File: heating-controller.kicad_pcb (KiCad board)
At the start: 2 copper layers, 0 parts

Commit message: Place and autoroute the board; add the reproducible routing pipeline
Board 150 x 95 mm, 2-layer, routed with Freerouting 2.5 from a placed
layout: DRC 0 violations / 0 unconnected, schematic parity clean, ERC clean.

- Isolation band, antenna keep-out, relay/opto slots, 6.4 mm mains-to-SELV
  custom DRC (heating-controller.kicad_dru) and MAINS / MAINS_SENSE / Power
  net classes in the project file.
- Fixed wiring laid before routing: L/N buses, relay COM/NO links,
  DEMAND_RET return, USB-C D+/D- bridges and VBUS escape, 31 GND stitching
  vias so the bottom pour stays in one piece.
- J115/J116 moved in from the board edge so every courtyard is inside the
  outline (JLC assembly margin).
- tools/route/: prep -> Freerouting -> SES import + pours -> DRC + gap fix,
  reproducible in ~2 min; outputs land in fab/route/ (ignored).
- Schematic: pin-type fixes in the project library, ESP32 thermal pads
  numbered; docs/design.md layout section rewritten to match the board.

Co-Authored-By: Claude Fable 5.1 <noreply@anthropic.com>
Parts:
- added C1: 1nF, Capacitor_SMD:C_0603_1608Metric, F.Cu at (32.5, 80.0)
- added C10: 100nF, Capacitor_SMD:C_0603_1608Metric, F.Cu at (132.5, 83.0)
- added C101: 1uF, Capacitor_SMD:C_0603_1608Metric, F.Cu at (97.0, 64.0)
- added C102: 1uF, Capacitor_SMD:C_0603_1608Metric, F.Cu at (106.0, 64.0)
- added C103: 1uF, Capacitor_SMD:C_0603_1608Metric, F.Cu at (115.0, 64.0)
- added C104: 1uF, Capacitor_SMD:C_0603_1608Metric, F.Cu at (124.0, 64.0)
- added C105: 1uF, Capacitor_SMD:C_0603_1608Metric, F.Cu at (133.0, 64.0)
- added C2: 470uF/16V, Capacitor_SMD:CP_Elec_8x10, F.Cu at (46.0, 76.0)
- added C3: 10uF, Capacitor_SMD:C_0805_2012Metric, F.Cu at (52.0, 76.0)
- added C4: 10uF, Capacitor_SMD:C_0805_2012Metric, F.Cu at (64.0, 76.0)
- added C5: 100nF, Capacitor_SMD:C_0603_1608Metric, F.Cu at (67.0, 76.0)
- added C6: 22uF, Capacitor_SMD:C_0805_2012Metric, F.Cu at (30.0, 68.0)
- added C7: 100nF, Capacitor_SMD:C_0603_1608Metric, F.Cu at (30.0, 72.0)
- added C8: 1uF, Capacitor_SMD:C_0603_1608Metric, F.Cu at (30.0, 63.0)
- added C9: 100nF, Capacitor_SMD:C_0603_1608Metric, F.Cu at (132.5, 77.0)
- added D1: SMF5.0A, Diode_SMD:D_SOD-123F, F.Cu at (53.0, 86.0)
- added D101: 1N4148WS, Diode_SMD:D_SOD-323, F.Cu at (35.0, 46.0)
- added D102: 1N4148WS, Diode_SMD:D_SOD-323, F.Cu at (52.0, 46.0)
- added D103: 1N4148WS, Diode_SMD:D_SOD-323, F.Cu at (69.0, 46.0)
- added D104: 1N4148WS, Diode_SMD:D_SOD-323, F.Cu at (86.0, 46.0)
- added D105: 1N4148WS, Diode_SMD:D_SOD-323, F.Cu at (97.0, 43.5)
- added D106: 1N4148WS, Diode_SMD:D_SOD-323, F.Cu at (106.0, 43.5)
- added D107: 1N4148WS, Diode_SMD:D_SOD-323, F.Cu at (115.0, 43.5)
- added D108: 1N4148WS, Diode_SMD:D_SOD-323, F.Cu at (124.0, 43.5)
- added D109: 1N4148WS, Diode_SMD:D_SOD-323, F.Cu at (133.0, 43.5)
- added D2: SMF5.0A, Diode_SMD:D_SOD-123F, F.Cu at (96.0, 84.0)
- added D201: 1N4148WS, Diode_SMD:D_SOD-323, F.Cu at (64.0, 58.0)
- added D202: 1N4148WS, Diode_SMD:D_SOD-323, F.Cu at (67.0, 58.0)
- added D203: 1N4148WS, Diode_SMD:D_SOD-323, F.Cu at (64.0, 63.0)
- added D204: 1N4148WS, Diode_SMD:D_SOD-323, F.Cu at (67.0, 63.0)
- added D205: 4V7 BZT52C4V7, Diode_SMD:D_SOD-123, F.Cu at (64.0, 70.0)
- added D206: 15V BZT52C15, Diode_SMD:D_SOD-123, F.Cu at (67.0, 70.0)
- added D207: 4V3 BZT52C4V3, Diode_SMD:D_SOD-123, F.Cu at (70.0, 70.0)
- added D208: SMAJ24A (DNP), Diode_SMD:D_SMA, F.Cu at (76.0, 72.0)
- added FID1: Fiducial_1mm_Mask3mm, Fiducial:Fiducial_1mm_Mask3mm, F.Cu at (8.00, 52.0)
- added FID2: Fiducial_1mm_Mask3mm, Fiducial:Fiducial_1mm_Mask3mm, F.Cu at (143.0, 60.0)
- added FID3: Fiducial_1mm_Mask3mm, Fiducial:Fiducial_1mm_Mask3mm, F.Cu at (58.0, 64.0)
- added H1: MountingHole_3.2mm_M3, MountingHole:MountingHole_3.2mm_M3, F.Cu at (4.00, 4.00)
- added H2: MountingHole_3.2mm_M3, MountingHole:MountingHole_3.2mm_M3, F.Cu at (146.0, 4.00)
- added H3: MountingHole_3.2mm_M3, MountingHole:MountingHole_3.2mm_M3, F.Cu at (4.00, 91.5)
- added H4: MountingHole_3.2mm_M3, MountingHole:MountingHole_3.2mm_M3, F.Cu at (146.0, 91.5)
- added J1: USB-C 16P, Connector_USB:USB_C_Receptacle_HRO_TYPE-C-31-M-12, F.Cu at (40.0, 90.5)
- added J110: MAINS IN L/N, jlc:CONN-TH_2P-P5.00_WJ128V-5.0-2P, F.Cu at (17.0, 8.00)
- added J111: K1 L/COM/NO, jlc:CONN-TH_3P-P5.00_WJ128V-5.0-3P, F.Cu at (32.0, 8.00)
- added J112: K2 L/COM/NO, jlc:CONN-TH_3P-P5.00_WJ128V-5.0-3P, F.Cu at (49.0, 8.00)
- added J113: K3 L/COM/NO, jlc:CONN-TH_3P-P5.00_WJ128V-5.0-3P, F.Cu at (66.0, 8.00)
- added J114: K4 L/COM/NO, jlc:CONN-TH_3P-P5.00_WJ128V-5.0-3P, F.Cu at (83.0, 8.00)
- added J115: END SW 1/2/3, jlc:CONN-TH_3P-P5.00_WJ128V-5.0-3P, F.Cu at (143.5, 37.0)
- added J116: DEMAND 230V/24V/RET, jlc:CONN-TH_3P-P5.00_WJ128V-5.0-3P, F.Cu at (143.5, 20.0)
- added J201: OT (24V max), jlc:CONN-TH_P3.50_KF350-3.5-2P, F.Cu at (58.0, 89.0)
- added J3: FLOW, jlc:CONN-TH_3P-P3.50_KF350-3.5-3P, F.Cu at (70.0, 89.0)
- added J4: OUTDOOR, jlc:CONN-TH_3P-P3.50_KF350-3.5-3P, F.Cu at (82.0, 89.0)
- added J5: OLED, Connector_PinHeader_2.54mm:PinHeader_1x04_P2.54mm_Vertical, F.Cu at (112.0, 88.0)
- added J6: QWIIC, Connector_JST:JST_SH_SM04B-SRSS-TB_1x04-1MP_P1.00mm_Horizontal, F.Cu at (98.0, 91.2)
- added J7: SPARE, Connector_PinHeader_2.54mm:PinHeader_1x04_P2.54mm_Vertical, F.Cu at (92.0, 80.0)
- added J8: BOOT_JP, Connector_PinHeader_2.54mm:PinHeader_1x02_P2.54mm_Vertical, F.Cu at (120.0, 71.0)
- added K101: HF32FA-G/005-HSL1, jlc:RELAY-TH_HF32FA-XX-HXX1X, F.Cu at (32.0, 33.0)
- added K102: HF32FA-G/005-HSL1, jlc:RELAY-TH_HF32FA-XX-HXX1X, F.Cu at (49.0, 33.0)
- added K103: HF32FA-G/005-HSL1, jlc:RELAY-TH_HF32FA-XX-HXX1X, F.Cu at (66.0, 33.0)
- added K104: HF32FA-G/005-HSL1 (DNP), jlc:RELAY-TH_HF32FA-XX-HXX1X, F.Cu at (83.0, 33.0)
- added LED1: STATUS, LED_SMD:LED_0603_1608Metric, F.Cu at (128.5, 56.0)
- added LED101: K1, LED_SMD:LED_0603_1608Metric, F.Cu at (35.0, 50.0)
- added LED102: K2, LED_SMD:LED_0603_1608Metric, F.Cu at (52.0, 50.0)
- added LED103: K3, LED_SMD:LED_0603_1608Metric, F.Cu at (69.0, 50.0)
- added LED104: K4, LED_SMD:LED_0603_1608Metric, F.Cu at (86.0, 50.0)
- added LED2: OT_ACT, LED_SMD:LED_0603_1608Metric, F.Cu at (128.5, 65.0)
- added Q101: AO3400A, Package_TO_SOT_SMD:SOT-23, F.Cu at (28.0, 46.0)
- added Q102: AO3400A, Package_TO_SOT_SMD:SOT-23, F.Cu at (45.0, 46.0)
- added Q103: AO3400A, Package_TO_SOT_SMD:SOT-23, F.Cu at (62.0, 46.0)
- added Q104: AO3400A, Package_TO_SOT_SMD:SOT-23, F.Cu at (79.0, 46.0)
- added Q201: S8550, Package_TO_SOT_SMD:SOT-23, F.Cu at (72.0, 60.0)
- added R1: 5.1k, Resistor_SMD:R_0603_1608Metric, F.Cu at (47.0, 86.0)
- added R10: 1k, Resistor_SMD:R_0603_1608Metric, F.Cu at (128.5, 68.0)
- added R11: 10k, Resistor_SMD:R_0603_1608Metric, F.Cu at (128.5, 71.0)
- added R110: 47k, Resistor_SMD:R_0603_1608Metric, F.Cu at (97.0, 61.0)
- added R111: 100, Resistor_SMD:R_0603_1608Metric, F.Cu at (24.0, 49.0)
- added R112: 100k, Resistor_SMD:R_0603_1608Metric, F.Cu at (28.0, 52.0)
- added R113: 1k, Resistor_SMD:R_0603_1608Metric, F.Cu at (34.0, 54.0)
- added R114: 22k, Resistor_SMD:R_1206_3216Metric, F.Cu at (95.0, 26.0)
- added R115: 22k, Resistor_SMD:R_1206_3216Metric, F.Cu at (95.0, 30.6)
- added R116: 22k, Resistor_SMD:R_1206_3216Metric, F.Cu at (95.0, 35.2)
- added R117: 22k, Resistor_SMD:R_1206_3216Metric, F.Cu at (99.0, 35.2)
- added R118: 22k, Resistor_SMD:R_1206_3216Metric, F.Cu at (99.0, 30.6)
- added R119: 22k, Resistor_SMD:R_1206_3216Metric, F.Cu at (99.0, 26.0)
- added R12: 4.7k, Resistor_SMD:R_0603_1608Metric, F.Cu at (110.0, 70.0)
- added R120: 47k, Resistor_SMD:R_0603_1608Metric, F.Cu at (106.0, 61.0)
- added R121: 100, Resistor_SMD:R_0603_1608Metric, F.Cu at (41.0, 49.0)
- added R122: 100k, Resistor_SMD:R_0603_1608Metric, F.Cu at (45.0, 52.0)
- added R123: 1k, Resistor_SMD:R_0603_1608Metric, F.Cu at (51.0, 54.0)
- added R124: 22k, Resistor_SMD:R_1206_3216Metric, F.Cu at (104.0, 26.0)
- added R125: 22k, Resistor_SMD:R_1206_3216Metric, F.Cu at (104.0, 30.6)
- added R126: 22k, Resistor_SMD:R_1206_3216Metric, F.Cu at (104.0, 35.2)
- added R127: 22k, Resistor_SMD:R_1206_3216Metric, F.Cu at (108.0, 35.2)
- added R128: 22k, Resistor_SMD:R_1206_3216Metric, F.Cu at (108.0, 30.6)
- added R129: 22k, Resistor_SMD:R_1206_3216Metric, F.Cu at (108.0, 26.0)
- added R13: 4.7k, Resistor_SMD:R_0603_1608Metric, F.Cu at (110.0, 73.0)
- added R130: 47k, Resistor_SMD:R_0603_1608Metric, F.Cu at (115.0, 61.0)
- added R131: 100, Resistor_SMD:R_0603_1608Metric, F.Cu at (58.0, 49.0)
- added R132: 100k, Resistor_SMD:R_0603_1608Metric, F.Cu at (62.0, 52.0)
- added R133: 1k, Resistor_SMD:R_0603_1608Metric, F.Cu at (68.0, 54.0)
- added R134: 22k, Resistor_SMD:R_1206_3216Metric, F.Cu at (113.0, 26.0)
- added R135: 22k, Resistor_SMD:R_1206_3216Metric, F.Cu at (113.0, 30.6)
- added R136: 22k, Resistor_SMD:R_1206_3216Metric, F.Cu at (113.0, 35.2)
- added R137: 22k, Resistor_SMD:R_1206_3216Metric, F.Cu at (117.0, 35.2)
- added R138: 22k, Resistor_SMD:R_1206_3216Metric, F.Cu at (117.0, 30.6)
- added R139: 22k, Resistor_SMD:R_1206_3216Metric, F.Cu at (117.0, 26.0)
- added R14: 4.7k, Resistor_SMD:R_0603_1608Metric, F.Cu at (76.0, 84.0)
- added R140: 47k, Resistor_SMD:R_0603_1608Metric, F.Cu at (124.0, 61.0)
- added R141: 100, Resistor_SMD:R_0603_1608Metric, F.Cu at (75.0, 49.0)
- added R142: 100k, Resistor_SMD:R_0603_1608Metric, F.Cu at (79.0, 52.0)
- added R143: 1k, Resistor_SMD:R_0603_1608Metric, F.Cu at (85.0, 54.0)
- added R144: 22k, Resistor_SMD:R_1206_3216Metric, F.Cu at (122.0, 26.0)
- added R145: 22k, Resistor_SMD:R_1206_3216Metric, F.Cu at (122.0, 30.6)
- added R146: 22k, Resistor_SMD:R_1206_3216Metric, F.Cu at (122.0, 35.2)
- added R147: 22k, Resistor_SMD:R_1206_3216Metric, F.Cu at (126.0, 35.2)
- added R148: 22k, Resistor_SMD:R_1206_3216Metric, F.Cu at (126.0, 30.6)
- added R149: 22k, Resistor_SMD:R_1206_3216Metric, F.Cu at (126.0, 26.0)
- added R15: 100, Resistor_SMD:R_0603_1608Metric, F.Cu at (80.0, 84.0)
- added R150: 47k, Resistor_SMD:R_0603_1608Metric, F.Cu at (133.0, 61.0)
- added R154: 22k, Resistor_SMD:R_1206_3216Metric, F.Cu at (131.0, 26.0)
- added R155: 22k, Resistor_SMD:R_1206_3216Metric, F.Cu at (131.0, 30.6)
- added R156: 22k, Resistor_SMD:R_1206_3216Metric, F.Cu at (131.0, 35.2)
- added R157: 22k, Resistor_SMD:R_1206_3216Metric, F.Cu at (135.0, 35.2)
- added R158: 22k, Resistor_SMD:R_1206_3216Metric, F.Cu at (135.0, 30.6)
- added R159: 22k, Resistor_SMD:R_1206_3216Metric, F.Cu at (135.0, 26.0)
- added R16: 0R, Resistor_SMD:R_0603_1608Metric, F.Cu at (110.0, 83.0)
- added R17: 0R (DNP), Resistor_SMD:R_0603_1608Metric, F.Cu at (113.0, 83.0)
- added R18: 0R, Resistor_SMD:R_0603_1608Metric, F.Cu at (116.0, 83.0)
- added R19: 0R (DNP), Resistor_SMD:R_0603_1608Metric, F.Cu at (119.0, 83.0)
- added R2: 5.1k, Resistor_SMD:R_0603_1608Metric, F.Cu at (49.5, 86.0)
- added R20: 0R, Resistor_SMD:R_0603_1608Metric, F.Cu at (122.0, 83.0)
- added R201: 330, Resistor_SMD:R_1206_3216Metric, F.Cu at (72.0, 65.0)
- added R202: 220, Resistor_SMD:R_0603_1608Metric, F.Cu at (76.0, 60.0)
- added R203: 100, Resistor_SMD:R_0603_1608Metric, F.Cu at (76.0, 65.0)
- added R204: 330, Resistor_SMD:R_0603_1608Metric, F.Cu at (92.0, 60.0)
- added R205: 1.5k, Resistor_SMD:R_0603_1608Metric, F.Cu at (92.0, 70.0)
- added R21: 0R (DNP), Resistor_SMD:R_0603_1608Metric, F.Cu at (125.0, 83.0)
- added R3: 1M, Resistor_SMD:R_0603_1608Metric, F.Cu at (35.0, 80.0)
- added R4: 10k, Resistor_SMD:R_0603_1608Metric, F.Cu at (30.0, 60.0)
- added R5: 10k, Resistor_SMD:R_0603_1608Metric, F.Cu at (30.0, 57.0)
- added R6: 10k, Resistor_SMD:R_0603_1608Metric, F.Cu at (132.5, 74.0)
- added R7: 10k, Resistor_SMD:R_0603_1608Metric, F.Cu at (132.5, 80.0)
- added R8: 1k, Resistor_SMD:R_0603_1608Metric, F.Cu at (128.5, 59.0)
- added R9: 10k, Resistor_SMD:R_0603_1608Metric, F.Cu at (128.5, 62.0)
- added SW1: RESET, jlc:SW-SMD_4P-L5.1-W5.1-P3.70-LS6.5-TL_H1.5, F.Cu at (120.0, 90.0)
- added SW2: BOOT, jlc:SW-SMD_4P-L5.1-W5.1-P3.70-LS6.5-TL_H1.5, F.Cu at (129.0, 90.0)
- added SW3: BTN1, jlc:SW-SMD_4P-L5.1-W5.1-P3.70-LS6.5-TL_H1.5, F.Cu at (138.0, 90.0)
- added SW4: BTN2, jlc:SW-SMD_4P-L5.1-W5.1-P3.70-LS6.5-TL_H1.5, F.Cu at (138.0, 80.0)
- added U1: ESP32-C6-WROOM-1-N8, jlc:WIRELM-SMD_ESP32-C6-WROOM-1, F.Cu at (17.0, 78.0)
- added U101: LTV-817S, jlc:OPTO-SMD-4_L4.6-W6.5-P2.54-LS10.3-BL, F.Cu at (97.0, 52.0)
- added U102: LTV-817S, jlc:OPTO-SMD-4_L4.6-W6.5-P2.54-LS10.3-BL, F.Cu at (106.0, 52.0)
- added U103: LTV-817S, jlc:OPTO-SMD-4_L4.6-W6.5-P2.54-LS10.3-BL, F.Cu at (115.0, 52.0)
- added U104: LTV-817S, jlc:OPTO-SMD-4_L4.6-W6.5-P2.54-LS10.3-BL, F.Cu at (124.0, 52.0)
- added U105: LTV-817S, jlc:OPTO-SMD-4_L4.6-W6.5-P2.54-LS10.3-BL, F.Cu at (133.0, 52.0)
- added U2: AMS1117-3.3, Package_TO_SOT_SMD:SOT-223-3_TabPin2, F.Cu at (58.0, 76.0)
- added U201: LTV-817S (TX), jlc:OPTO-SMD-4_L4.6-W6.5-P2.54-LS10.3-BL, F.Cu at (87.0, 62.0)
- added U202: LTV-817S (RX), jlc:OPTO-SMD-4_L4.6-W6.5-P2.54-LS10.3-BL, F.Cu at (87.0, 76.0)
- added U3: USBLC6-2SC6, Package_TO_SOT_SMD:SOT-23-6, F.Cu at (40.0, 83.0)
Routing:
- net GND: track 0.00 -> 723.5 mm, vias 0 -> 36
- net +5V: track 0.00 -> 286.7 mm, vias 0 -> 12
- net +3V3: track 0.00 -> 272.0 mm, vias 0 -> 5
- net /MAINS_OK: track 0.00 -> 193.5 mm, vias 0 -> 2
- net /Power + MCU/BTN1: track 0.00 -> 164.9 mm, vias 0 -> 5
- net /DEMAND_IN: track 0.00 -> 164.0 mm, vias 0 -> 4
- net /Power + MCU/LED_OT: track 0.00 -> 160.2 mm, vias 0 -> 5
- net /Power + MCU/BOOT: track 0.00 -> 155.9 mm, vias 0 -> 2
- net /Mains IO/MAINS_N: track 0.00 -> 153.7 mm, vias 0 -> 9
- net /Mains IO/MAINS_L: track 0.00 -> 150.8 mm, vias 0 -> 2
- net /Power + MCU/EN: track 0.00 -> 143.5 mm, vias 0 -> 6
- net /Power + MCU/BTN2: track 0.00 -> 138.6 mm, vias 0 -> 4
- net /Power + MCU/LED_STATUS: track 0.00 -> 132.8 mm, vias 0 -> 2
- net /ES3: track 0.00 -> 129.6 mm, vias 0 -> 2
- net /Power + MCU/SPARE17: track 0.00 -> 126.5 mm, vias 0 -> 4
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- added copper zone on B.Cu, net GND
- added copper zone on F.Cu, net GND
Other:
- board outline added: 150 x 95 mm

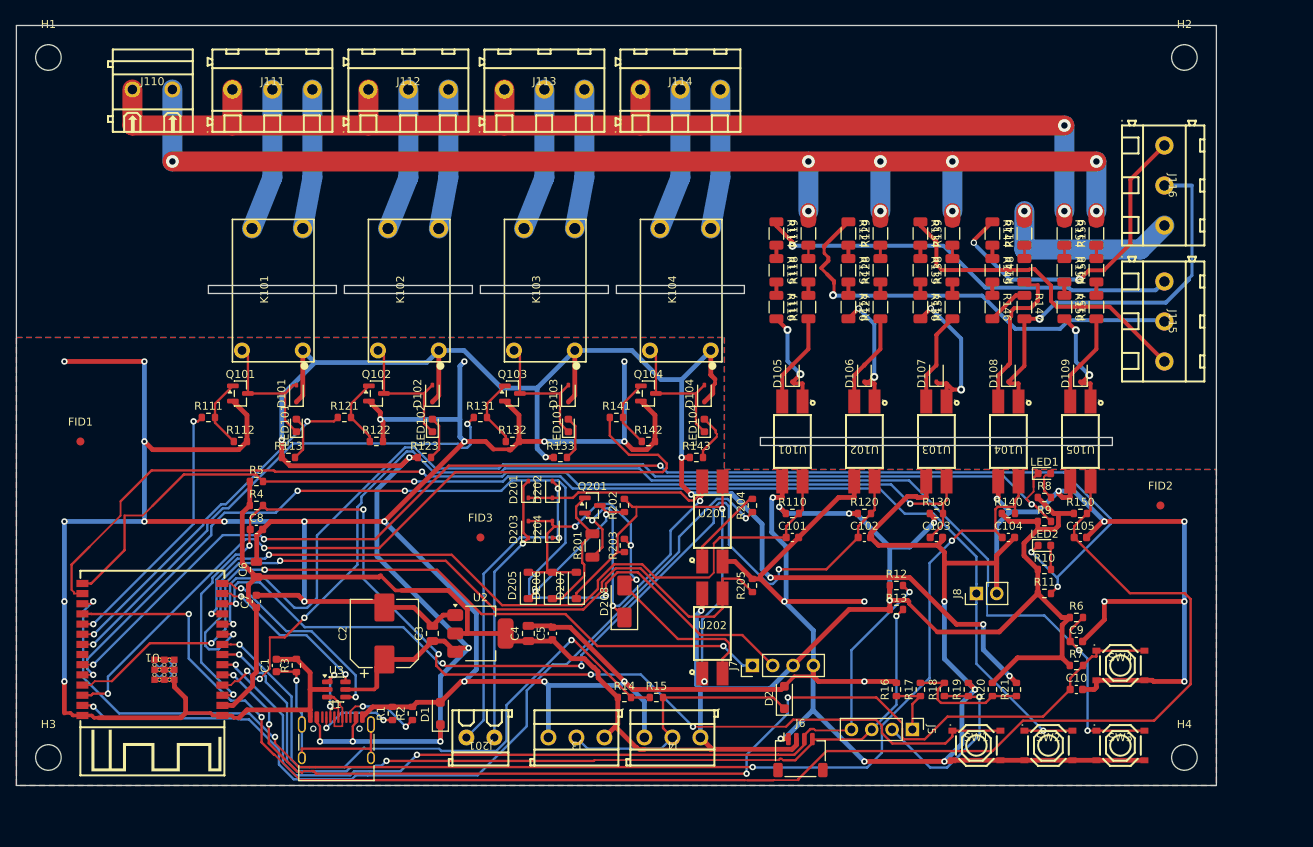
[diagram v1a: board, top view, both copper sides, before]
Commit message: Address the independent design review: OT net split and fuse, 2.0 mm live-input class, demand detector margin, 3V3 copper, silkscreen
Two review rounds closed with design changes rather than prose:

- OpenTherm: U201 emitter and D207 cathode moved off OT_N1 onto OT_TXE
  (the net merge echoed our own TX into the RX opto); D208 SMAJ24A fitted;
  F201 1 A 250 V fast 2410 fuse in series with OT1 so a 230 V miswire is a
  calculable TVS-plus-fuse crowbar instead of parts failing open.
- Raw live inputs (ES1-3_IN, DEMAND_230) in a MAINS_IN class at 2.0 mm to
  everything, included in the 6.4 mm and edge rules; mains-to-mains 2.0 mm;
  the four inputs are pre-routed as locked lanes (the autorouter cannot
  thread them at that clearance); J115 wired ES3/ES2/ES1 top to bottom.
- Demand chain 3+3 and opto pull-ups 220 k after a time-domain model showed
  the 24 V detector had no margin; R15 330 R limits 1-Wire clamp current.
- +3V3 copper on the regulator tab (locked bars + pour, 125 mm2); GND island
  repair vias and stitching cleanup in the pipeline; silkscreen labels at
  every terminal pin plus warnings; LCSC/Description/Datasheet copied into
  the PCB footprints so schematic parity is clean (7 board-only items).
- Docs: design.md and requirements.md corrected where they had drifted;
  docs/layout-notes.md records what worked and failed in routing and margins.

Board: DRC 0 errors / 0 unconnected, ERC 0 errors, courtyards inside the
outline, Freerouting 40 passes in ~1 min.

Co-Authored-By: Claude Fable 5.1 <noreply@anthropic.com>
Claude-Session: https://claude.ai/code/session_01XDSh2Z4phxf7z2Gu1153CL
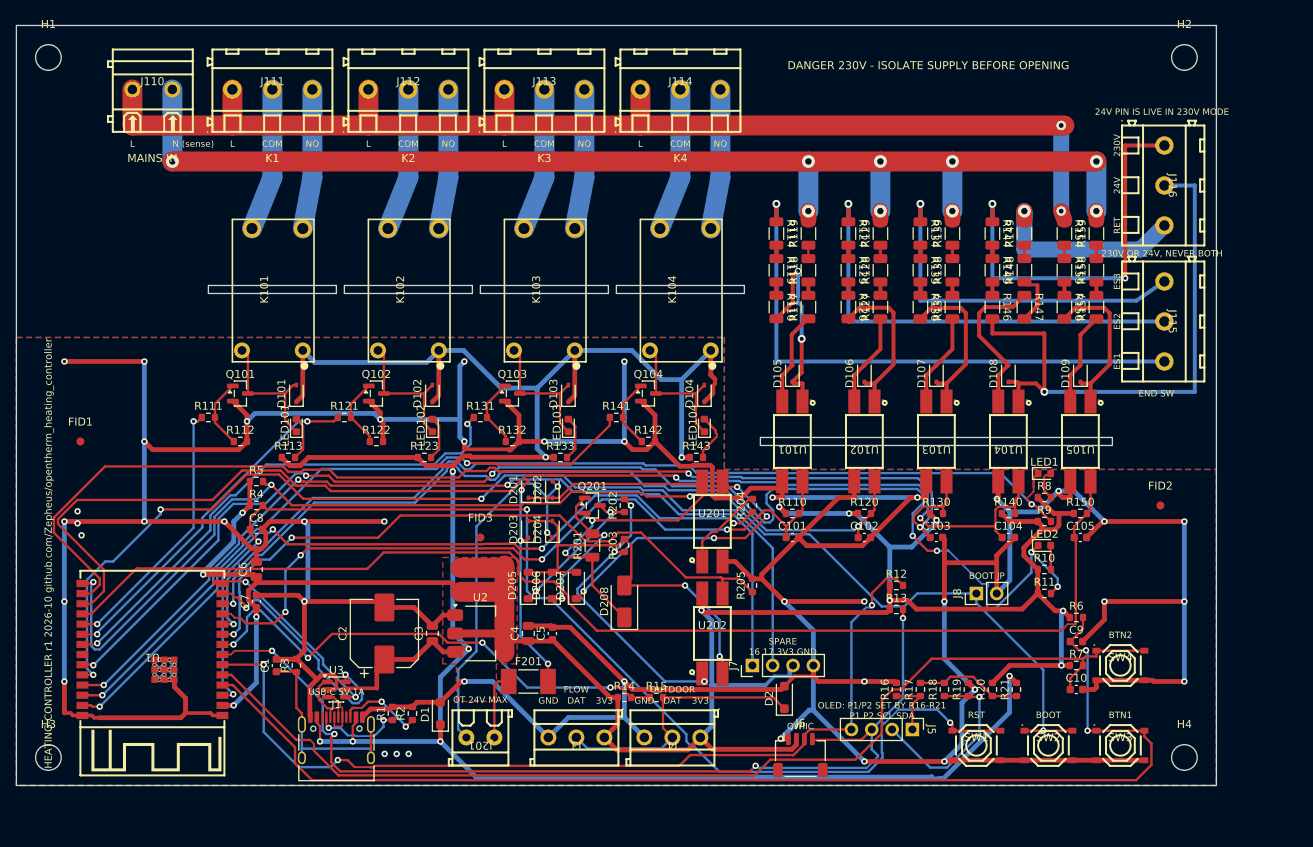
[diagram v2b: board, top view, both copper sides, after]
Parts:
- added F201: 1A 250V fast, Fuse:Fuse_Littelfuse-NANO2-451_453, F.Cu at (64.0, 82.0)
- D208: value SMAJ24A (DNP) -> SMAJ24A
- R110, R120, R130, R140, R150: value 47k -> 220k
- R15: value 100 -> 330
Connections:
- D207 pad 1: /OpenTherm/OT_N1 -> /OpenTherm/OT_TXE
- J115 pad 1: /Mains IO/ES1_IN -> /Mains IO/ES3_IN
- J115 pad 3: /Mains IO/ES3_IN -> /Mains IO/ES1_IN
- J201 pad 1: /OpenTherm/OT1 -> /OpenTherm/OT1_IN
- R146 pad 2: /Mains IO/S4_3 -> /Mains IO/DEMAND_24
- R147 pad 1: /Mains IO/S4_3 -> /Mains IO/LEDK4
- R147 pad 2: /Mains IO/DEMAND_24 -> /Mains IO/S4_3
- R148 pad 1: /Mains IO/LEDK4 -> /Mains IO/S4_3
- U201 pad 3: /OpenTherm/OT_N1 -> /OpenTherm/OT_TXE
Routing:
- net /MAINS_OK: track 193.5 -> 152.0 mm, vias 2 -> 0
- net /OpenTherm/OT_TXE: track 0.00 -> 35.4 mm, vias 0 -> 4
- net +3V3: track 272.0 -> 303.1 mm, vias 5 -> 11
- net /Mains IO/DEMAND_24: track 50.3 -> 71.3 mm
- net +5V: track 286.7 -> 305.1 mm, vias 12 -> 8
- net /OpenTherm/OT_N1: track 55.4 -> 37.7 mm, vias 2 -> 3
- net /Mains IO/ES1_IN: track 53.1 -> 70.4 mm
- net /Power + MCU/SPARE16: track 98.0 -> 115.1 mm
- net /RLY4: track 98.4 -> 82.5 mm
- net /ES3: track 129.6 -> 145.2 mm
- net /Power + MCU/BTN1: track 164.9 -> 151.0 mm, vias 5 -> 2
- net /Power + MCU/ONEWIRE: track 77.0 -> 63.2 mm, vias 2 -> 4
- net /ES2: track 114.7 -> 101.0 mm, vias 4 -> 2
- net /OT_IN: track 94.8 -> 82.7 mm
- net /Mains IO/LEDA1: track 13.2 -> 25.2 mm
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- added copper zone on F.Cu, net +3V3
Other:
- board text added: "16 17 3V3 GND"
- board text added: "230V"
- board text added: "230V OR 24V, NEVER BOTH"
- board text added: "24V"
- board text added: "24V PIN IS LIVE IN 230V MODE"
- board text added: "3V3"
- board text added: "BOOT"
- board text added: "BOOT JP"
- board text added: "BTN1"
- board text added: "BTN2"
- board text added: "COM"
- board text added: "DANGER 230V - ISOLATE SUPPLY BEFORE OPENING"
- board text added: "DAT"
- board text added: "END SW"
- board text added: "ES1"
- board text added: "ES2"
- board text added: "ES3"
- board text added: "FLOW"
- board text added: "GND"
- board text added: "HEATING-CONTROLLER r1 2026-10 github.com/Zepheus/opentherm_heating_controller"
- board text added: "K1"
- board text added: "K2"
- board text added: "K3"
- board text added: "K4"
- board text added: "L"
- board text added: "MAINS IN"
- board text added: "N (sense)"
- board text added: "NO"
- board text added: "OLED: P1/P2 SET BY R16-R21"
- board text added: "OT 24V MAX"
- board text added: "OUTDOOR"
- board text added: "P1 P2 SCL SDA"
- board text added: "QWIIC"
- board text added: "RET"
- board text added: "RST"
- board text added: "SPARE"
- board text added: "USB-C 5V 1A"

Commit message: Name the board Andiron v1.0; add BOM with cost estimates, renders, getting-started docs and CLAUDE.md
- Andiron v1.0 and the author name on the silkscreen, in every title block
  and in the README; J116 warning moved inside the board edge.
- tools/bom.py: BOM from the schematic with LCSC prices from the Konnect
  JLCPCB database -> docs/BOM.md (cost summary, Basic/Extended, DNP list) and
  docs/bom/andiron-bom-jlc.csv (JLCPCB upload). ~$15.77 components per board,
  ~$28.97 per board at 5 including assumed Extended-part fees.
- tools/sync_models.py relinks all 152 footprints to 3D models with portable
  ${KIPRJMOD} paths (also fixed in lib/jlc.pretty); stand-ins for the
  ESP32-C6 module and HRO USB-C. Wired into the routing pipeline.
- tools/render.sh: ray-traced 3D views and 2D layer plots in docs/images/.
- README rewritten: renders, BOM summary, getting started with Konnect MCP,
  repository layout. tools/README.md indexes every script; Konnect helpers
  and the pour-island check moved into tools/.
- CLAUDE.md: BOM and cost estimate kept current on every schematic change,
  definition of done for board changes.
- .konnect/project.json design rules brought in line with what is built;
  project-local .mcp.json for Konnect.
- Removed references to a commercial product; the docs now describe the
  board on its own terms, designed for Home Assistant and ESPHome.

ERC 0 errors; DRC 0 errors, 0 unconnected, parity clean.

Co-Authored-By: Claude Opus 5.5 <noreply@anthropic.com>
Claude-Session: https://claude.ai/code/session_01XDSh2Z4phxf7z2Gu1153CL
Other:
- board text added: "ANDIRON v1.0"
- board text added: "Cedric Van Goethem 2026"
- board text added: "DEMAND: 230V OR 24V"
- board text added: "IS LIVE IN 230V MODE"
- board text added: "NEVER BOTH. 24V PIN"
- board text added: "github.com/Zepheus/opentherm_heating_controller"
- board text removed: "230V OR 24V, NEVER BOTH"
- board text removed: "24V PIN IS LIVE IN 230V MODE"
- board text removed: "HEATING-CONTROLLER r1 2026-10 github.com/Zepheus/opentherm_heating_controller"

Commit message: Final sanity pass: decoupling moved to the module pin, spacing spec checked every run, creepage DRC, licence, README for humans
Sanity check (pinouts, connectivity, routing, manufacturability):
- ESP32-C6-WROOM-1 pin table, USB D-/D+ on GPIO12/13, strapping pins
  (GPIO8/9/15 pulled up, EN 10k/1uF) and every active/polarised part's
  pinout verified against datasheets; no changes needed.
- Decoupling: C6 (22uF) and C7 (100nF) moved from 17/13 mm to 3.0/1.5 mm
  from the module's 3V3 pin. The pipeline now starts from the committed
  placed board tools/route/placed.kicad_pcb.
- Creepage rule (6.4 mm mains-to-SELV, follows slots) added to the DRC file;
  verified live by tightening it until it failed (actual minimum ~8.8 mm).
- tools/check/spacing_rules.json: every isolation/spacing limit with its
  basis; tools/check/sanity.py verifies the DRC file encodes each one, plus
  rule areas, slots, JLC drill/annular limits, decoupling distances, antenna
  keep-out. The pipeline runs it last and it passes.
- tools/route/clean_dangling.py removes Freerouting's dangling vias/stubs
  that DRC reports, reverting any pass that would disconnect something.
- Docs: OT_IN description corrected; R10.6 spacing requirement; layout
  lessons appended; README trimmed for human readers, name removed, cost
  estimate dated; 2D plots shipped as PNG (SVGs did not display on GitHub).
- Licence: CERN-OHL-P-2.0 for the hardware, MIT for the scripts.

ERC 0 errors; DRC 0 errors, 0 unconnected, parity clean; sanity PASS.
BOM unchanged: ~$15.77 components per board, ~$28.97 per board at 5.

Co-Authored-By: Claude Opus 5.5 <noreply@anthropic.com>
Claude-Session: https://claude.ai/code/session_01XDSh2Z4phxf7z2Gu1153CL
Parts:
- moved C6 14.6 mm to (28.4, 82.5), turned to 0 degrees
- moved C7 13.2 mm to (28.0, 85.0), turned to 0 degrees
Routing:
- net +5V: track 305.1 -> 272.9 mm
- net /OT_OUT: track 99.9 -> 122.6 mm, vias 4 -> 2
- net /MAINS_OK: track 152.0 -> 170.4 mm, vias 0 -> 4
- net /ES2: track 101.0 -> 115.6 mm, vias 2 -> 4
- net /OpenTherm/OT_GND: track 51.5 -> 66.0 mm, vias 2 -> 0
- net /OpenTherm/OT_VP: track 58.8 -> 44.6 mm
- net /Power + MCU/BOOT: track 166.7 -> 154.7 mm
- net /Power + MCU/USB_DP: track 26.8 -> 38.5 mm
- net /Power + MCU/SPARE17: track 126.0 -> 116.0 mm, vias 3 -> 1
- net /OpenTherm/OT_TXE: track 35.4 -> 25.5 mm, vias 4 -> 2
- net /Power + MCU/USB_DN: track 29.8 -> 20.5 mm
- net /Power + MCU/USB_SHIELD: track 27.5 -> 36.5 mm
- net /Power + MCU/SDA: track 115.7 -> 106.9 mm
- net /Power + MCU/SPARE16: track 115.1 -> 107.1 mm
- net /RLY4: track 82.5 -> 90.5 mm
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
